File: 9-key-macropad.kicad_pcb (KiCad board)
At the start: 2 copper layers, 57.4 x 57.4 mm, 20 parts, among them SW1 SW_Push, SW2 SW_Push, SW3 SW_Push, SW4 SW_Push, SW5 SW_Push, SW6 SW_Push, SW7 SW_Push, SW8 SW_Push, SW9 SW_Push, U1 XIAO-RP2040-DIP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

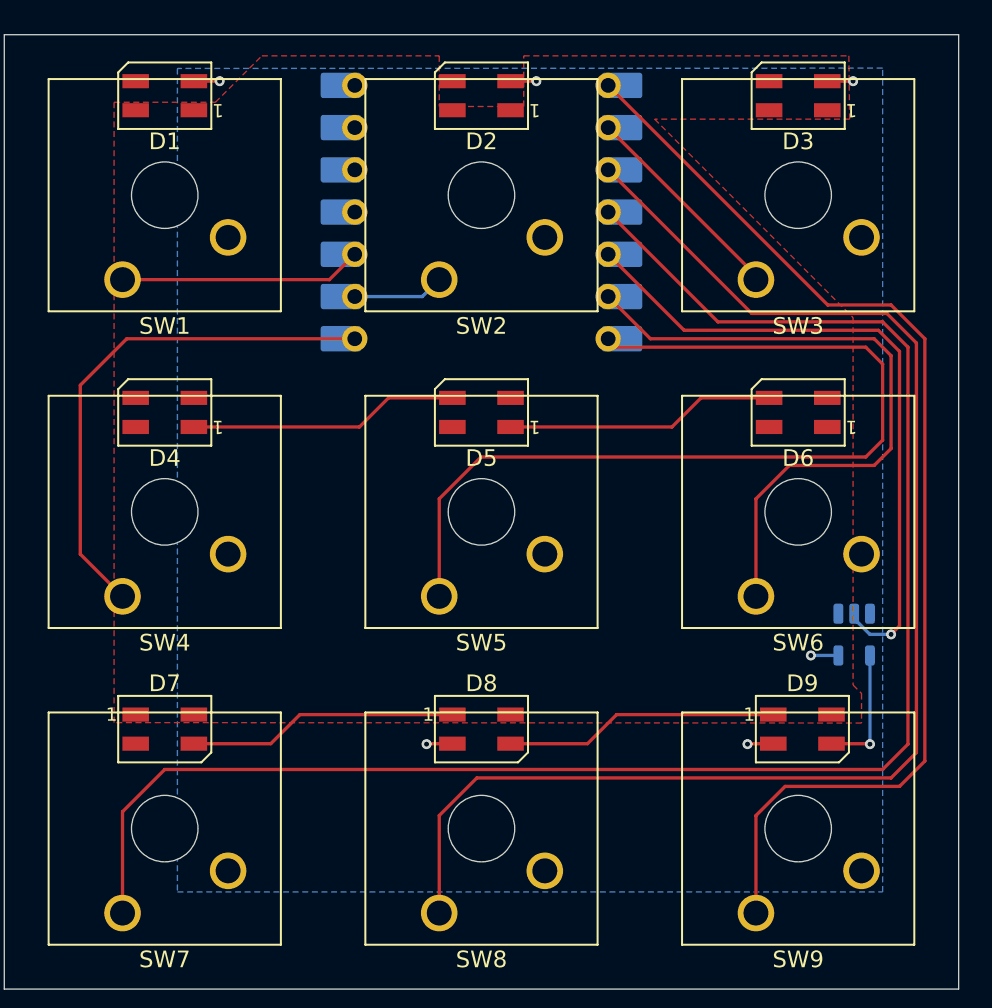
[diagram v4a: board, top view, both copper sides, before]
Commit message: PCB and schematic design complete pending review
Completed the design for the PCB and Schematic.

Holding off having it printed until I can find a professional to review it.
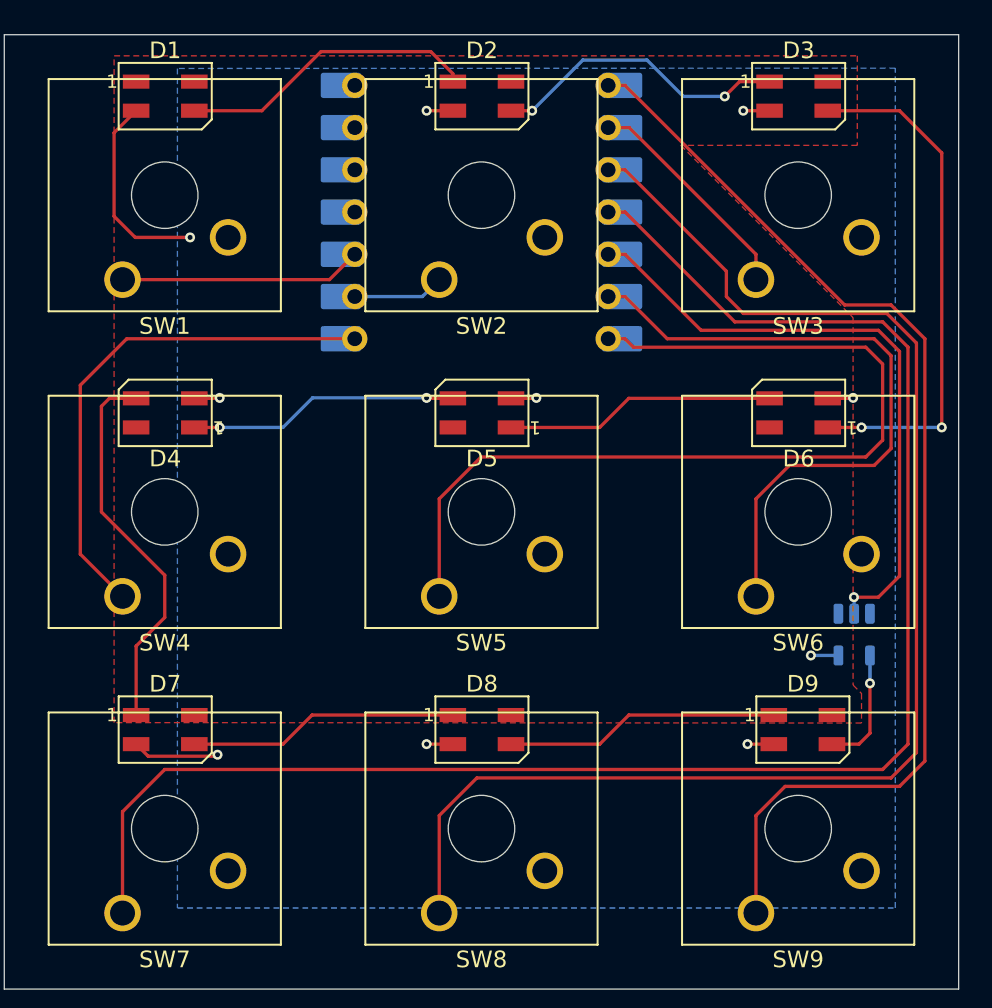
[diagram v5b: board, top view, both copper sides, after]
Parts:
- turned D1 to 0 degrees
- turned D2 to 0 degrees
- turned D3 to 0 degrees
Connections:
- D1 pad 3: unconnected-(D1-DIN-Pad3) -> Net-(D1-DIN)
- D2 pad 1: unconnected-(D2-DOUT-Pad1) -> Net-(D1-DIN)
- D2 pad 3: unconnected-(D2-DIN-Pad3) -> Net-(D2-DIN)
- D3 pad 1: unconnected-(D3-DOUT-Pad1) -> Net-(D2-DIN)
- D3 pad 3: unconnected-(D3-DIN-Pad3) -> Net-(D3-DIN)
- D6 pad 1: unconnected-(D6-DOUT-Pad1) -> Net-(D3-DIN)
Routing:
- net Net-(D3-DIN): track 0.00 -> 31.3 mm, vias 0 -> 2
- net Net-(D4-DIN): track 0.00 -> 23.1 mm
- net GNDD: track 7.78 -> 28.2 mm, vias 5 -> 9
- net Net-(D2-DIN): track 0.00 -> 18.1 mm, vias 0 -> 2
- net Net-(D1-DIN): track 0.00 -> 18.1 mm
- net NEOPIX: track 40.1 -> 38.0 mm
- net KEY8: track 83.6 -> 84.5 mm
- net KEY3: track 12.8 -> 13.6 mm
- net Net-(D4-DOUT): vias 0 -> 2
